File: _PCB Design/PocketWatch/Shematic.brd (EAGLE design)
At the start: 53 x 58 mm, 42 parts, among them U2 ATTINY88-AU

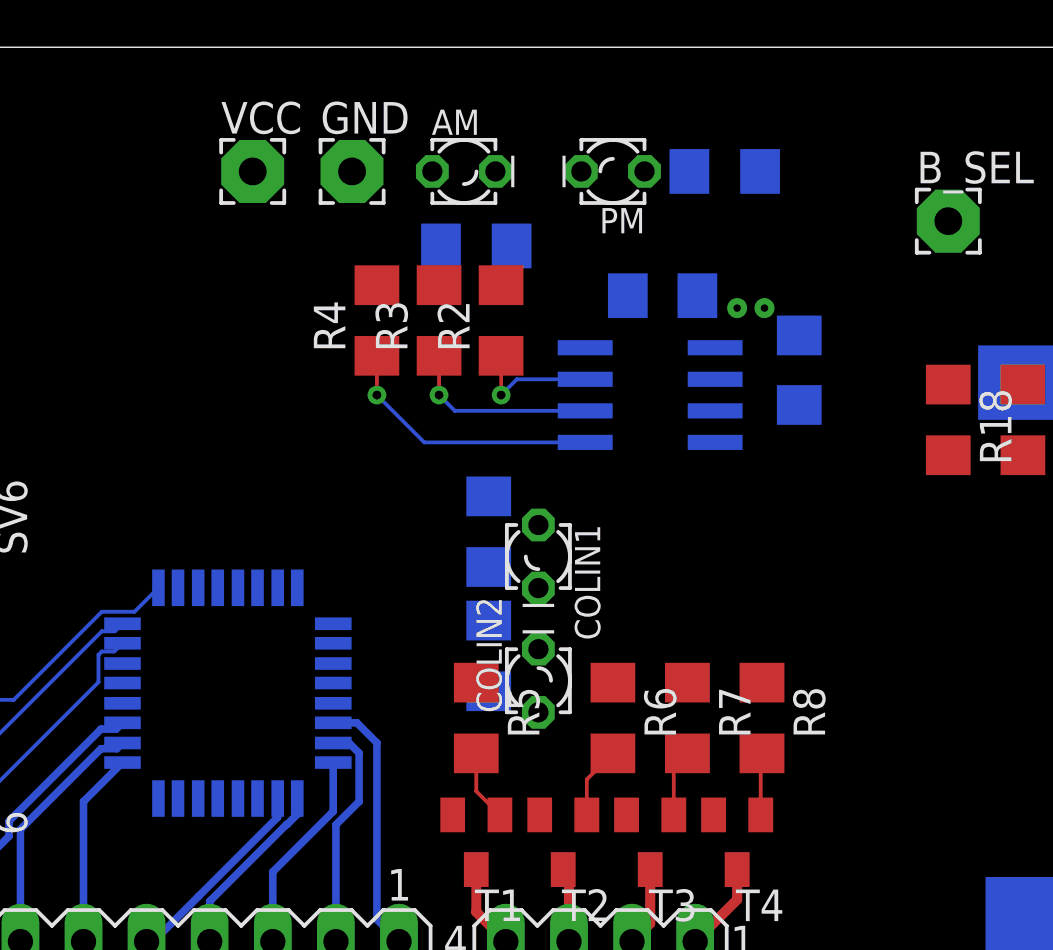
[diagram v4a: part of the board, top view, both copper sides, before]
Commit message: Refined layout, routed more traces
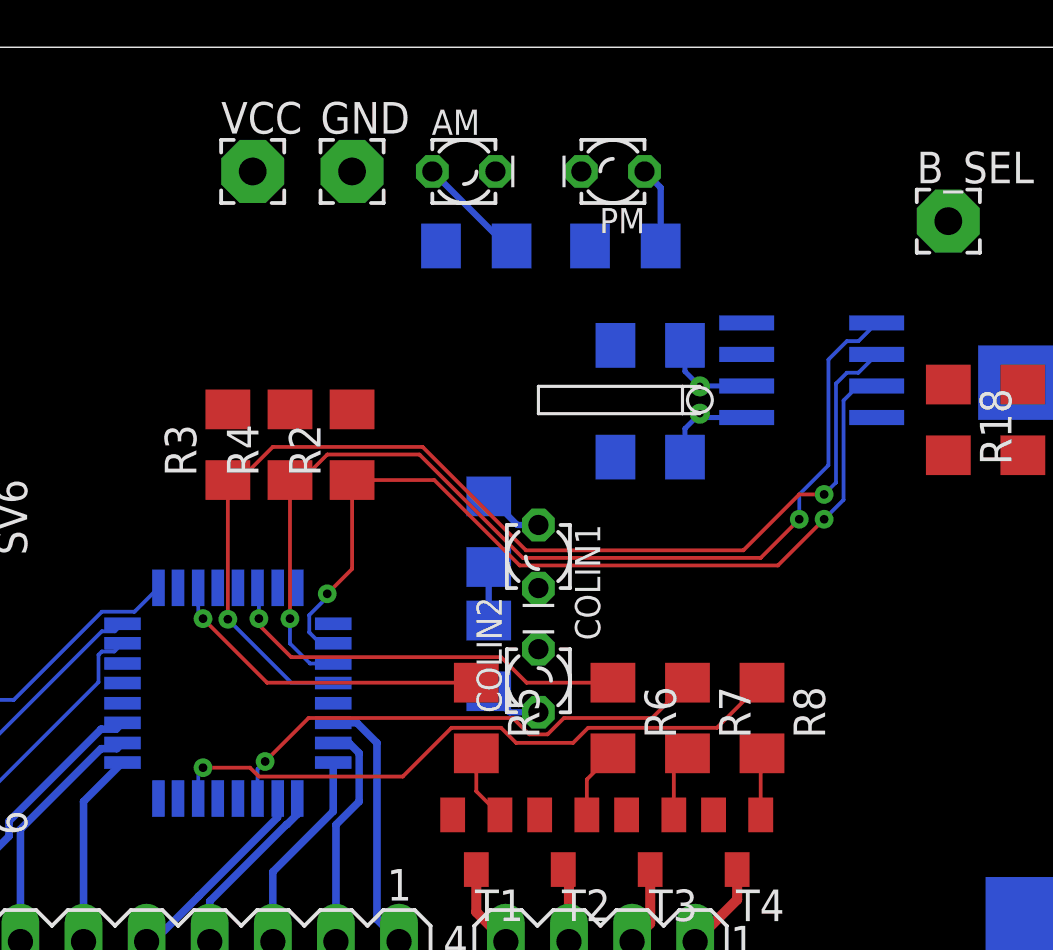
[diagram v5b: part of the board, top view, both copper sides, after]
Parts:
- moved R3 9.86 mm to (14.0, 42.0)
- moved R2 7.81 mm to (19.0, 42.0)
- moved MCP7940M 6.58 mm to (37.5, 45.0), turned to 90 degrees
- moved C2 6.52 mm to (31.0, 41.5)
- moved R4 6.10 mm to (16.5, 42.0)
- moved C1 6.08 mm to (31.0, 46.0), turned to 0 degrees
- moved R17 5.00 mm to (30.0, 50.0), turned to 0 degrees
- moved 6PF 4.51 mm to (33.0, 43.2), flipped to the top, turned to 90 degrees
- turned R16 to 0 degrees
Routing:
- net SCL: track 7.72 -> 44.9 mm, vias 1 -> 2
- net SDA: track 10.8 -> 41.4 mm, vias 1 -> 2
- net MFP: track 5.22 -> 35.9 mm, vias 1 -> 2
- net EN3: track 0.00 -> 26.0 mm, vias 0 -> 1
- net EN2: track 0.00 -> 20.5 mm, vias 0 -> 1
- net EN1: track 0.00 -> 16.7 mm, vias 0 -> 1
- net EN0: track 0.00 -> 13.4 mm, vias 0 -> 1
- net N$12: track 0.00 -> 4.43 mm
- net N$6: track 0.00 -> 3.95 mm
- net N$4: track 0.00 -> 3.79 mm
- net N$14: track 0.00 -> 3.27 mm
- net N$7: track 0.00 -> 2.48 mm
- net N$9: track 0.00 -> 2.35 mm
- net N$15: track 0.00 -> 2.16 mm

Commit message: Update
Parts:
- added TGND, TGND2: WIREPAD2,54/1,1, wirepad:2,54/1,1
- moved GND 1.00 mm to (18.0, 53.0)
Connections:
- new net TGND: TGND.1
- net GND: now also TGND2.1
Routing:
- net TG3_2: track 20.3 -> 21.4 mm
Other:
- board size 53 x 58 mm -> 53 x 56 mm
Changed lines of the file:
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@@
 <plain>
 <wire x1="0" y1="0" x2="53" y2="0" width="0" layer="20"/>
-<wire x1="53" y1="19" x2="53" y2="58" width="0" layer="20"/>
-<wire x1="53" y1="58" x2="0" y2="58" width="0" layer="20"/>
-<wire x1="0" y1="58" x2="0" y2="19" width="0" layer="20"/>
+<wire x1="53" y1="19" x2="53" y2="56" width="0" layer="20"/>
+<wire x1="53" y1="56" x2="0" y2="56" width="0" layer="20"/>
+<wire x1="0" y1="56" x2="0" y2="19" width="0" layer="20"/>
 <wire x1="0" y1="18" x2="0" y2="0" width="0" layer="20"/>
 <wire x1="53" y1="0" x2="53" y2="18" width="0" layer="20"/>
@@
 <element name="MCP7940M" library="smd-footprints" package="SOIC-8" value="SOIC-8" x="37.5" y="45" rot="MR90"/>
 <element name="VCC" library="wirepad" library_urn="urn:adsk.eagle:library:412" package="2,54/1,1" package3d_urn="urn:adsk.eagle:package:30836/1" value="WIREPAD2,54/1,1" x="15" y="53"/>
-<element name="GND" library="wirepad" library_urn="urn:adsk.eagle:library:412" package="2,54/1,1" package3d_urn="urn:adsk.eagle:package:30836/1" value="WIREPAD2,54/1,1" x="19" y="53"/>
 <element name="B_SEL" library="wirepad" library_urn="urn:adsk.eagle:library:412" package="2,54/1,1" package3d_urn="urn:adsk.eagle:package:30836/1" value="WIREPAD" x="43" y="51"/>
 <element name="B_UP" library="wirepad" library_urn="urn:adsk.eagle:library:412" package="2,54/1,1" package3d_urn="urn:adsk.eagle:package:30836/1" value="WIREPAD" x="49" y="48"/>
@@
 <attribute name="SUPPLIER" value="ATMEL" x="14" y="32" size="1.778" layer="28" rot="MR90" display="off"/>
 </element>
+<element name="TGND" library="wirepad" library_urn="urn:adsk.eagle:library:412" package="2,54/1,1" package3d_urn="urn:adsk.eagle:package:30836/1" value="WIREPAD2,54/1,1" x="38" y="15"/>
+<element name="TGND2" library="wirepad" library_urn="urn:adsk.eagle:library:412" package="2,54/1,1" package3d_urn="urn:adsk.eagle:package:30836/1" value="WIREPAD2,54/1,1" x="38" y="22"/>
+<element name="GND" library="wirepad" library_urn="urn:adsk.eagle:library:412" package="2,54/1,1" package3d_urn="urn:adsk.eagle:package:30836/1" value="WIREPAD2,54/1,1" x="18" y="53"/>
 </elements>
 <signals>
@@
 <contactref element="T4" pad="E"/>
 <contactref element="SV6" pad="1"/>
-<contactref element="GND" pad="1"/>
 <contactref element="COLIN1" pad="K"/>
 <contactref element="PM" pad="K"/>
 <contactref element="AM" pad="K"/>
 <contactref element="COLIN2" pad="K"/>
+<contactref element="TGND2" pad="1"/>
+<contactref element="GND" pad="1"/>
 <wire x1="29.6" y1="46" x2="34.8838" y2="46.905" width="0" layer="19" extent="16-16"/>
 <wire x1="29.6" y1="41.5" x2="29.6" y2="46" width="0" layer="19" extent="16-16"/>
@@
 <wire x1="33.55" y1="27.1" x2="30.05" y2="27.1" width="0" layer="19" extent="1-1"/>
 <wire x1="23.05" y1="27.1" x2="26.55" y2="27.1" width="0" layer="19" extent="1-1"/>
+<wire x1="38" y1="22" x2="33.55" y2="27.1" width="0" layer="19" extent="1-1"/>
 <wire x1="28.23" y1="53" x2="29.6" y2="46" width="0" layer="19" extent="16-16"/>
 <wire x1="24.77" y1="53" x2="28.23" y2="53" width="0" layer="19" extent="1-1"/>
-<wire x1="19" y1="53" x2="24.77" y2="53" width="0" layer="19" extent="1-1"/>
+<wire x1="46" y1="23.1" x2="38" y2="22" width="0" layer="19" extent="16-16"/>
 <wire x1="13.5936" y1="27.7582" x2="23.05" y2="27.1" width="0" layer="19" extent="1-16"/>
 <wire x1="14.4064" y1="36.2418" x2="13.5936" y2="27.7582" width="0" layer="19" extent="16-16"/>
 <wire x1="3" y1="39.35" x2="14.4064" y2="36.2418" width="0" layer="19" extent="16-16"/>
-<wire x1="46" y1="23.1" x2="33.55" y2="27.1" width="0" layer="19" extent="1-16"/>
+<wire x1="18" y1="53" x2="13.5936" y2="27.7582" width="0" layer="19" extent="16-16"/>
 </signal>
 <signal name="VCC">
@@
 <contactref element="TUBE3" pad="1"/>
 <contactref element="SV3" pad="1"/>
-<wire x1="42.1221" y1="8.9046375" x2="42.1221" y2="8.8779" width="0.4064" layer="16"/>
-<wire x1="42.1221" y1="8.8779" x2="46" y2="5" width="0.4064" layer="16"/>
-<wire x1="32.81" y1="15" x2="36.0267375" y2="15" width="0.4064" layer="16"/>
-<wire x1="36.0267375" y1="15" x2="42.1221" y2="8.9046375" width="0.4064" layer="16"/>
-<wire x1="46" y1="5" x2="46" y2="2.0056" width="0.4064" layer="16"/>
+<wire x1="37.8779" y1="5.0953625" x2="37.8779" y2="5.1221" width="0.4064" layer="16"/>
+<wire x1="46" y1="2.0056" x2="40.9676625" y2="2.0056" width="0.4064" layer="16"/>
+<wire x1="40.9676625" y1="2.0056" x2="37.8779" y2="5.0953625" width="0.4064" layer="16"/>
+<wire x1="32.81" y1="10.19" x2="32.81" y2="15" width="0.4064" layer="16"/>
+<wire x1="37.8779" y1="5.1221" x2="32.81" y2="10.19" width="0.4064" layer="16"/>
 </signal>
 <signal name="TG0">
@@
 <wire x1="9.7582" y1="32.4064" x2="22.578" y2="50" width="0" layer="19" extent="16-16"/>
 </signal>
+<signal name="TGND">
+<contactref element="TGND" pad="1"/>
+</signal>
 </signals>

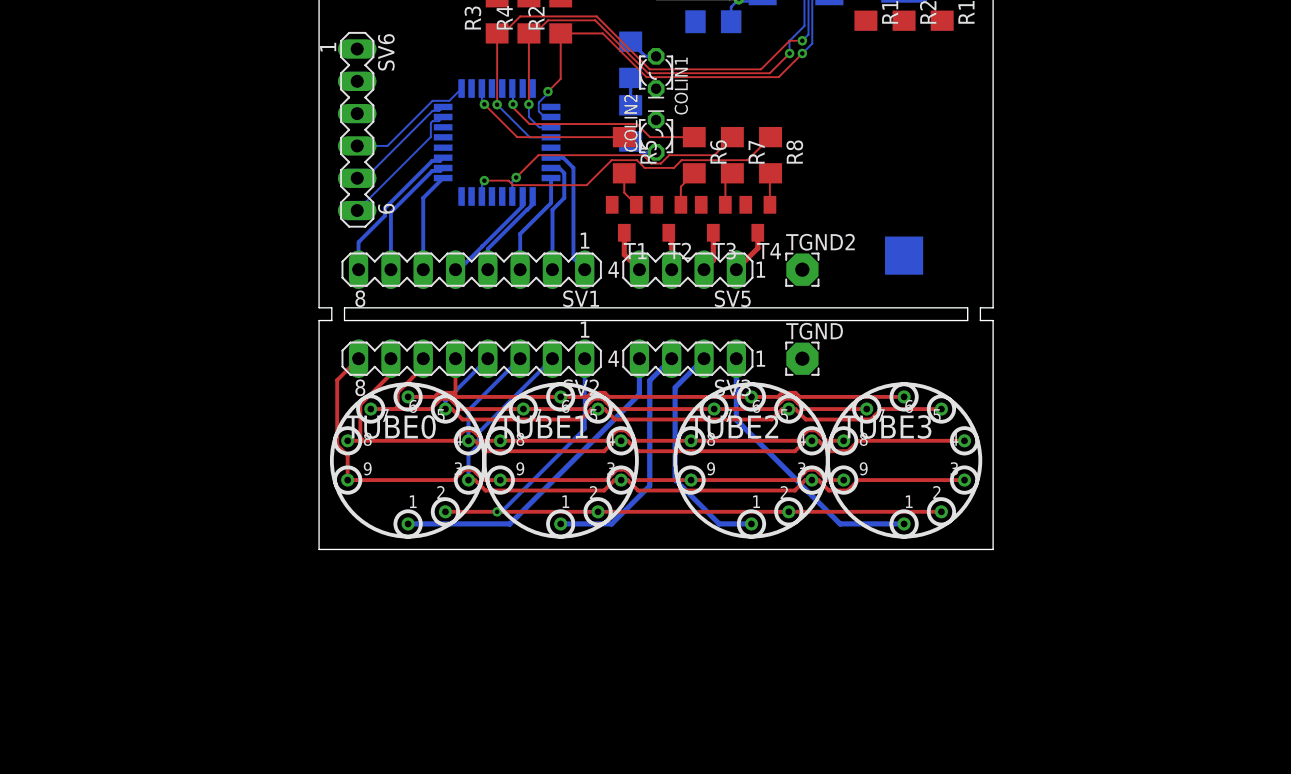
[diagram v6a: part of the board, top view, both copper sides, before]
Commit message: Changed Tube common to positive voltage. Changed to multiplexer design base (Frees up pins for motor control).
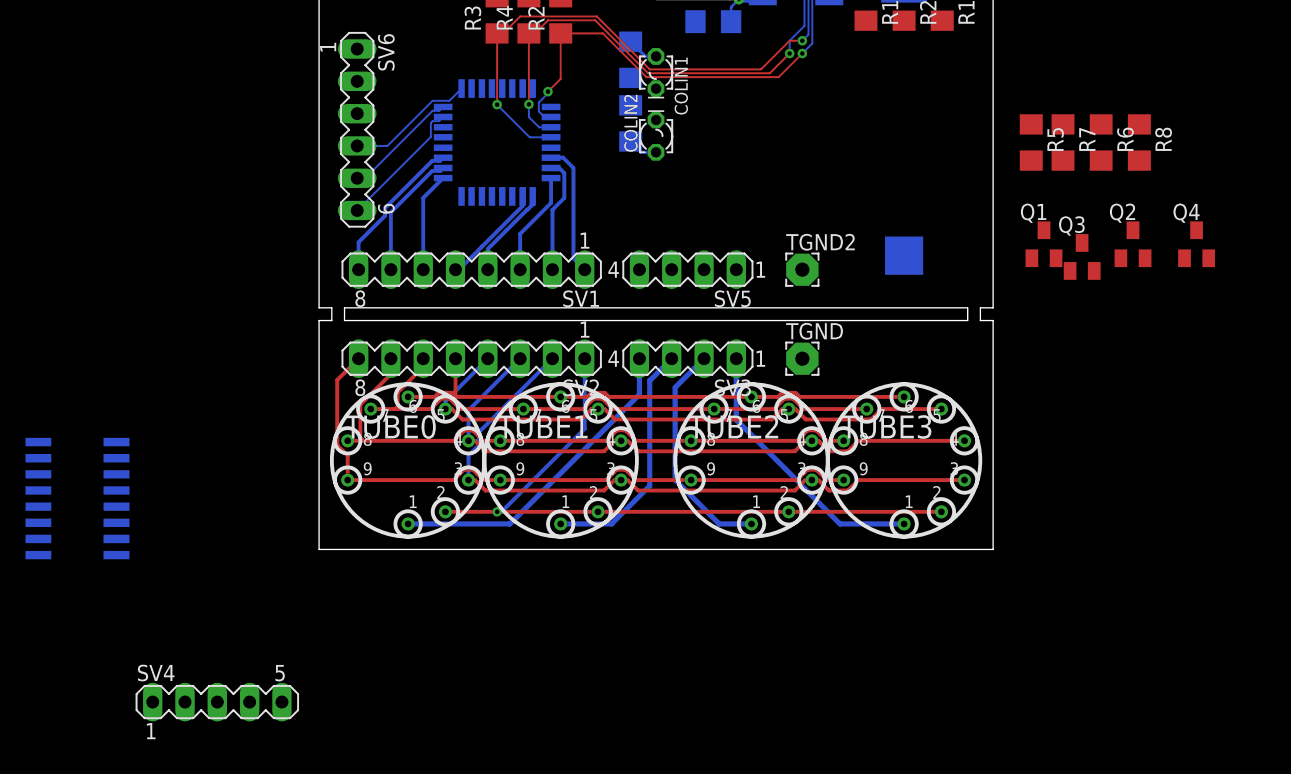
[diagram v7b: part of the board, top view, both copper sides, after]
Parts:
- removed T1, T2, T3, T4: (no value), transistor:SOT23-BEC
- added IC1: 74HC139D, 74xx-eu:SO16
- added Q1, Q2, Q3, Q4: BCX71SMD, transistor-pnp:SOT23
- added SV4: (no value), con-lstb:MA05-1
- moved R5 32.0 mm to (56.0, 32.0)
- moved R6 32.0 mm to (61.5, 32.0)
- moved R8 29.0 mm to (64.5, 32.0)
- moved R7 26.0 mm to (58.5, 32.0)
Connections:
- net TG0_2 renamed T0_2
- net TG1_2 renamed T1_2
- net TG2_2 renamed T2_2
- net TG3_2 renamed T3_2
- removed net EN0: R5.1, U2.19
- removed net EN1: R6.1, U2.22
- removed net EN2: R7.1, U2.3
- removed net EN3: R8.1, U2.6
- removed net TG0: SV5.4, T1.C
- removed net TG1: SV5.3, T2.C
- removed net TG2: SV5.2, T3.C
- removed net TG3: SV5.1, T4.C
- new net LEDC0: IC1.13, U2.3
- new net LEDC1: IC1.14, U2.6
- new net N$10: IC1.5, R6.1
- new net N$11: IC1.6, R7.1
- new net N$13: IC1.7, R8.1
- new net N$18: IC1.9, R14.2
- new net N$8: IC1.4, R5.1
- new net T0: Q1.3, SV5.4
- new net T1: Q2.3, SV5.3
- new net T2: Q3.3, SV5.2
- new net T3: Q4.3, SV5.1
- new net TC0: IC1.2, U2.19
- new net TC1: IC1.3, U2.22
- net GND: now also IC1.1, IC1.15, IC1.8; no longer AM.K, COLIN1.K, COLIN2.K, PM.K, T1.E, T2.E, T3.E, T4.E
- net N$1: now also Q4.1; no longer T4.B
- net N$15: now also IC1.12, R17.2; no longer R14.2, R15.2, U2.12
- net N$16: now also IC1.11, R16.2; no longer R17.2, U2.14
- net N$17: now also IC1.10, R15.2; no longer R16.2, U2.13
- net N$2: now also Q3.1; no longer T3.B
- net N$3: now also Q2.1; no longer T2.B
- net N$5: now also Q1.1; no longer T1.B
- net VCC: now also AM.K, COLIN1.K, COLIN2.K, IC1.16, PM.K, Q1.2, Q2.2, Q3.2, Q4.2
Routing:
- net EN3: track 26.0 -> 0.00 mm, vias 1 -> 0
- net EN2: track 20.5 -> 0.00 mm, vias 1 -> 0
- net EN1: track 16.7 -> 0.00 mm, vias 1 -> 0
- net EN0: track 13.4 -> 0.00 mm, vias 1 -> 0
- net TG3: track 3.60 -> 0.00 mm
- net TG0: track 3.39 -> 0.00 mm
- net TG2: track 3.20 -> 0.00 mm
- net TG1: track 3.00 -> 0.00 mm
- net N$3: track 2.91 -> 0.00 mm
- net N$5: track 2.87 -> 0.00 mm
- net N$2: track 2.71 -> 0.00 mm
- net N$1: track 2.50 -> 0.00 mm
- net N$15: track 2.16 -> 0.00 mm

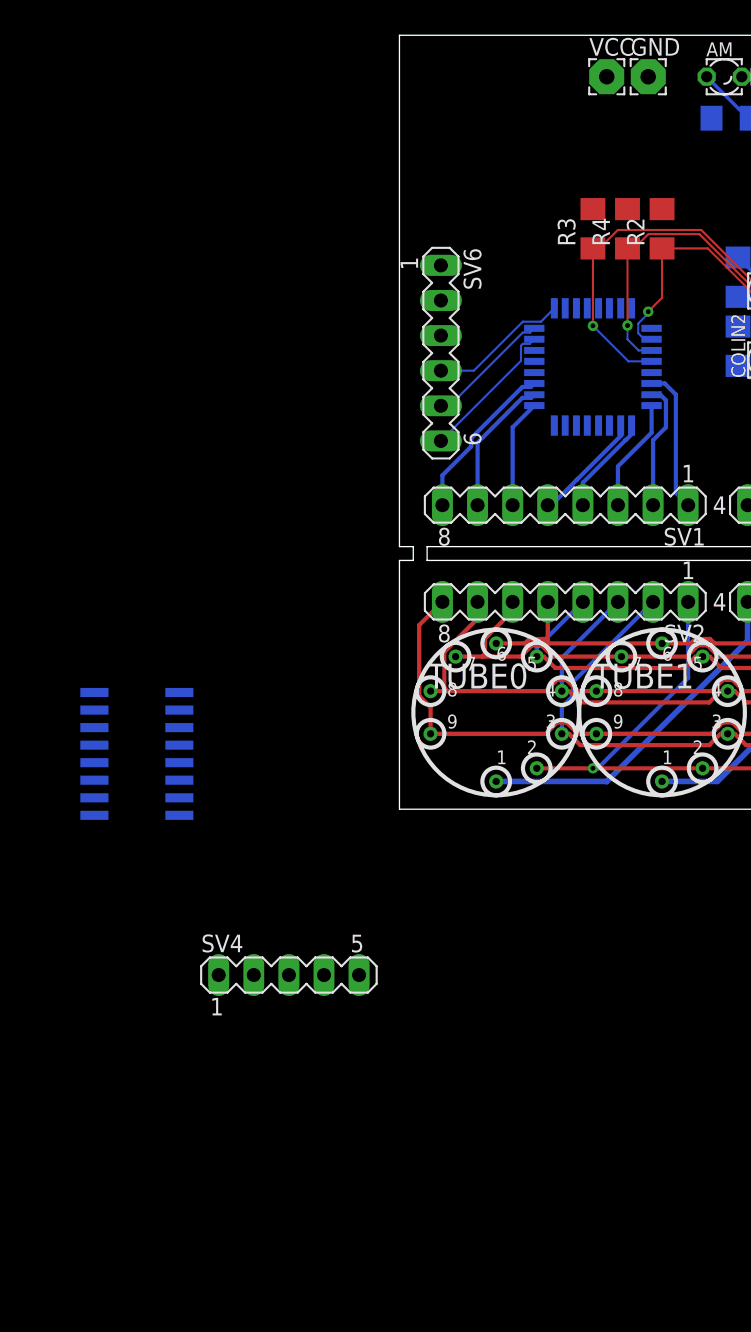
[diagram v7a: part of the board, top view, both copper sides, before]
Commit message: Added Motor drive circuitry. Rearranged pin connections
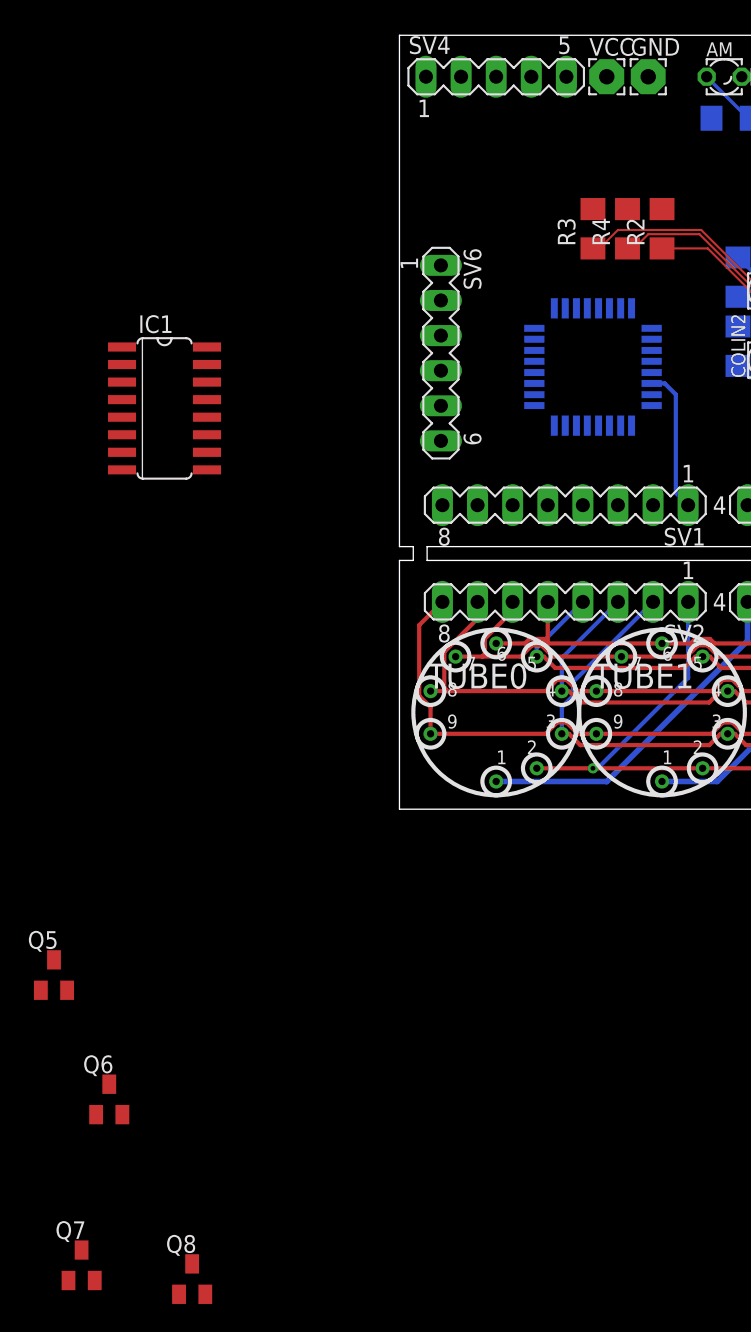
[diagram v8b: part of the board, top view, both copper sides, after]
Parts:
- added Q5, Q6, Q7, Q8: (no value), transistor-npn:SOT23
- moved SV4 66.7 mm to (7.00, 53.0)
- moved IC1 25.1 mm to (-17.0, 29.0), flipped to the top
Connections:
- removed net LEDC0: IC1.13, U2.3
- removed net LEDC1: IC1.14, U2.6
- new net HEF: U2.20
- new net M0: Q5.1, U2.19
- new net M1: Q6.1, U2.22
- new net M2: Q7.1, U2.3
- new net M3: Q8.1, U2.6
- new net N$19: Q5.3, SV4.1
- new net N$20: Q6.3, SV4.2
- new net N$21: Q7.3, SV4.3
- new net N$22: Q8.3, SV4.4
- new net N$27: IC1.13, U2.7
- new net N$28: IC1.14, U2.8
- net GND: now also Q5.2, Q6.2, Q7.2, Q8.2
- net TC0: now also U2.12; no longer U2.19
- net TC1: now also U2.13; no longer U2.22
- net VCC: now also SV4.5
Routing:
- net SEG_G: track 11.9 -> 0.00 mm
- net SCL: track 44.9 -> 34.0 mm, vias 2 -> 1
- net MOSI: track 10.4 -> 0.00 mm
- net SCK: track 10.1 -> 0.00 mm
- net SEG_F: track 10.1 -> 0.00 mm
- net SEG_A: track 9.18 -> 0.00 mm
- net MISO: track 9.08 -> 0.00 mm
- net SDA: track 41.4 -> 32.8 mm, vias 2 -> 1
- net SEG_B: track 8.21 -> 0.00 mm
- net SEG_D: track 8.10 -> 0.00 mm
- net MFP: track 35.9 -> 27.9 mm, vias 2 -> 1
- net SEG_E: track 7.86 -> 0.00 mm
- net SEG_C: track 7.23 -> 0.00 mm
